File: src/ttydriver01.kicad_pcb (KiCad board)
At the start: 2 copper layers, 119.4 x 74.9 mm, 34 parts, among them P1 CONN_01X04, P2 CONN_01X02, P3 CONN_01X02, P4 CONN_01X10, Q1 IRLB8721PBF, T1 Coilcraft-DA2032, U1 NE555, U2 TPS2030P, U3 CP2102-breakout, U4 G3VM401E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

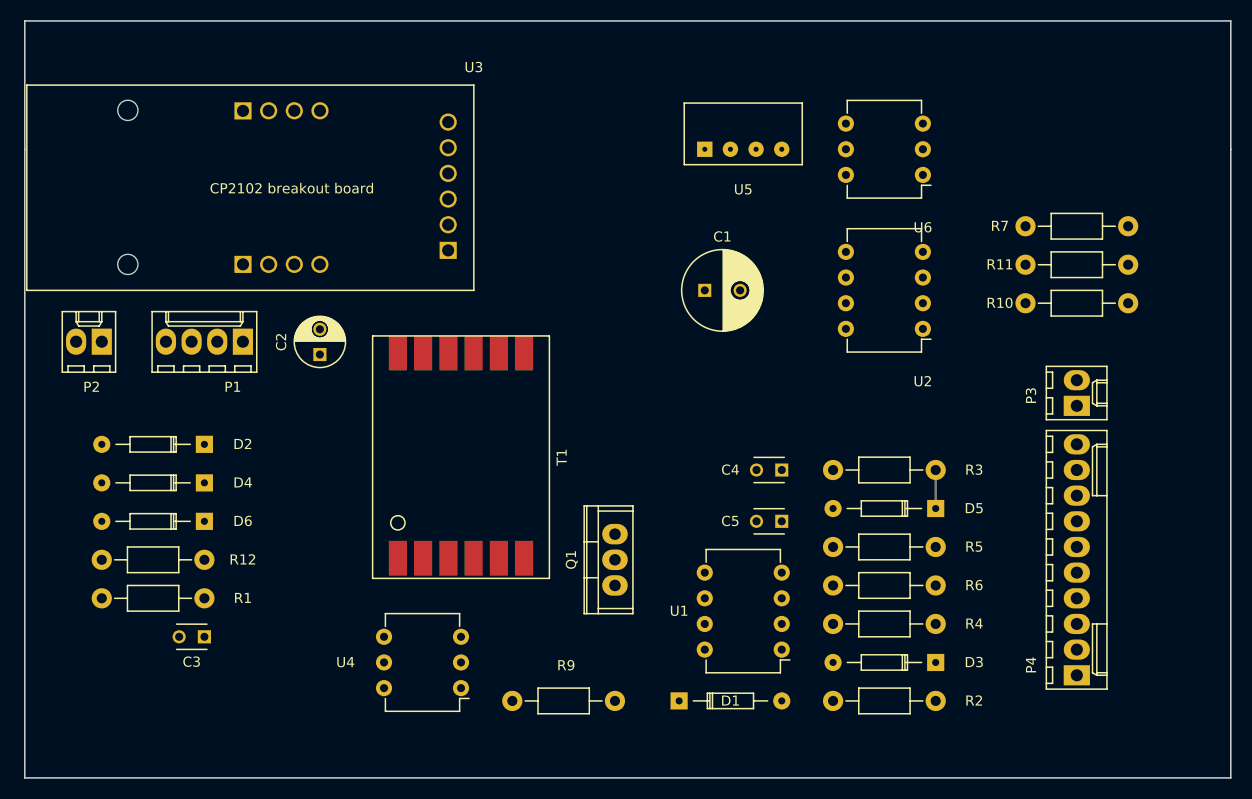
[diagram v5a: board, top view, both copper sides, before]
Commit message: Add GND fill area. Still no tracks
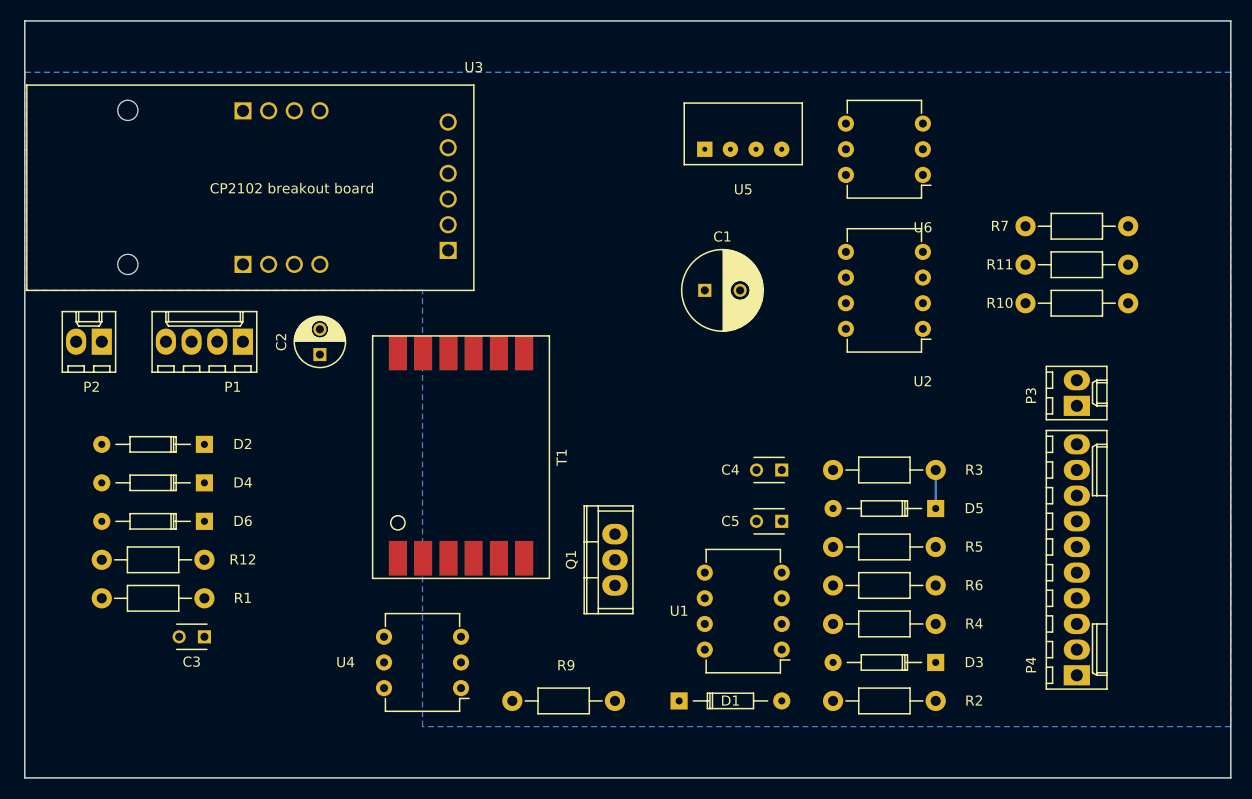
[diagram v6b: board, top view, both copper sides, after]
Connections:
- net //SUSPEND renamed /ENABLE
- net Net-(C2-Pad2) renamed /HVNEG
- net Net-(C3-Pad1) renamed /HVPOS
- net Net-(Q1-Pad3) renamed /OSC
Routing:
- added copper zone on B.Cu, net GND

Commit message: New smaller pads for connectors.  HV part laid out.
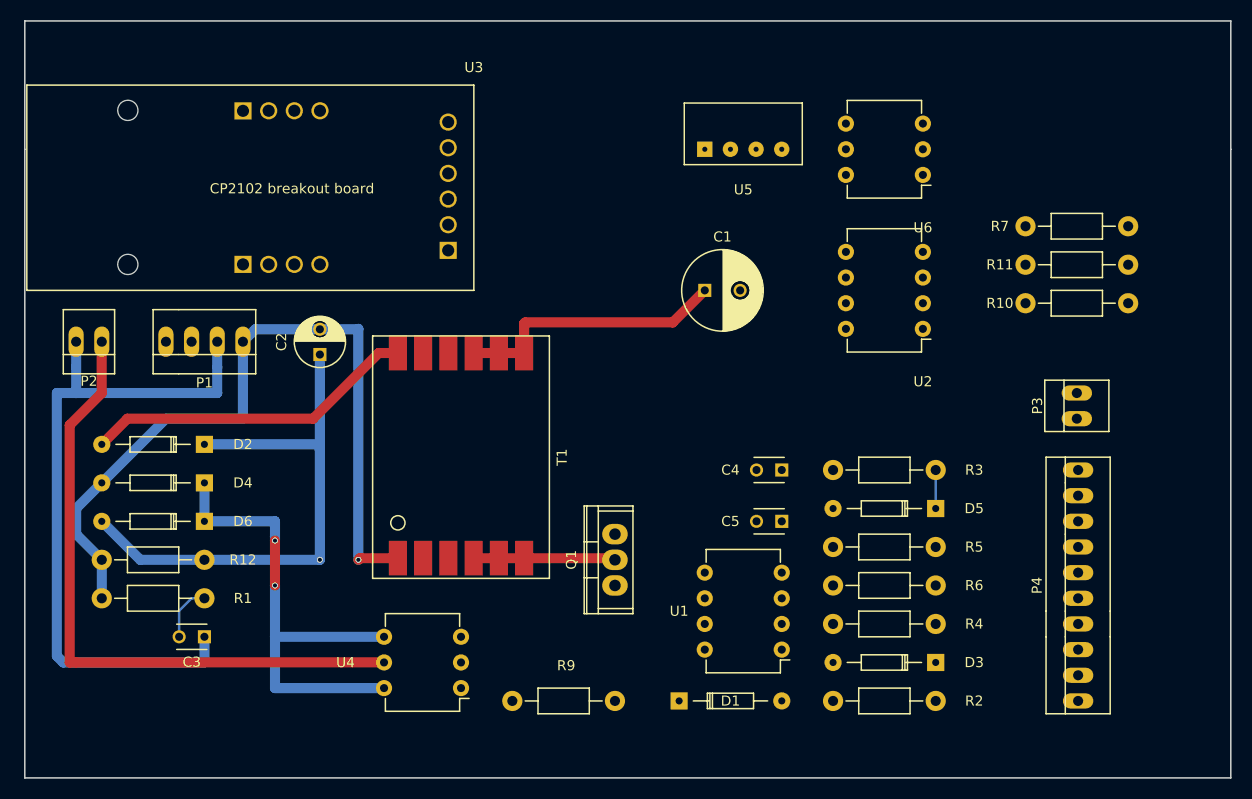
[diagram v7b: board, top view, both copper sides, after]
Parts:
- P1: footprint Connectors_Molex:Molex_KK-6410-04_04x2.54mm_Straight -> DC-DC:PINHEAD1-4
- P2, P3: footprint Connectors_Molex:Molex_KK-6410-02_02x2.54mm_Straight -> Connect:PINHEAD1-2
- P4: footprint Connectors_Molex:Molex_KK-6410-10_10x2.54mm_Straight -> DC-DC:PINHEAD1-10
- moved P4 8.89 mm to (160.0, 133.3)
- moved P1 3.81 mm to (73.7, 109.2)
- moved P2 1.27 mm to (62.2, 109.2)
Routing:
- net /HVNEG: track 0.00 -> 79.5 mm, vias 0 -> 1
- net /HVPOS: track 0.00 -> 69.5 mm
- net Net-(P2-Pad1): track 0.00 -> 64.2 mm
- net Net-(C2-Pad1): track 0.00 -> 55.6 mm, vias 0 -> 1
- net Net-(D4-Pad1): track 0.00 -> 48.9 mm, vias 0 -> 2
- net Net-(D2-Pad2): track 0.00 -> 34.2 mm
- net Net-(C1-Pad1): track 0.00 -> 27.2 mm
- net Net-(Q1-Pad2): track 0.00 -> 14.1 mm
- net Net-(C3-Pad2): track 0.00 -> 5.59 mm
- removed copper zone on B.Cu, net GND
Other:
- net class PWR: clearance 0.5 -> 0.6

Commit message: All traces in place; now to begin cleanup
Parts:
- Q1: footprint Power_Integrations:TO-220 -> DC-DC:TO-220-HV
- moved P3 97.4 mm to (62.9, 109.2), turned to 180 degrees
- moved P2 34.6 mm to (85.7, 134.6)
- moved Q1 1.27 mm to (113.0, 130.8)
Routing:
- net Net-(P3-Pad2): track 0.00 -> 169.7 mm
- net VCC: track 0.00 -> 157.6 mm, vias 0 -> 3
- net Net-(P4-Pad6): track 0.00 -> 132.6 mm, vias 0 -> 1
- net Net-(P4-Pad3): track 0.00 -> 114.8 mm, vias 0 -> 2
- net Net-(P4-Pad1): track 0.00 -> 99.0 mm
- net /RxD: track 0.00 -> 95.3 mm, vias 0 -> 3
- net Net-(P1-Pad4): track 0.00 -> 90.3 mm, vias 0 -> 2
- net /ENABLE: track 0.00 -> 78.3 mm, vias 0 -> 3
- net Net-(P1-Pad3): track 0.00 -> 66.9 mm
- net /TxD: track 0.00 -> 65.7 mm, vias 0 -> 2
- net Net-(D3-Pad2): track 0.00 -> 64.1 mm, vias 0 -> 1
- net Net-(P2-Pad1): track 64.2 -> 10.4 mm
- net Net-(P4-Pad2): track 0.00 -> 49.7 mm
- net Net-(C1-Pad1): track 27.2 -> 67.2 mm, vias 0 -> 1
- net Net-(P4-Pad9): track 0.00 -> 31.6 mm
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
